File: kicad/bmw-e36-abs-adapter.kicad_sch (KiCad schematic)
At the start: 41 parts, among them J1 TE_9-6437287-8, J2 SWD, U1 TPSM33610S5, U2 TLV73333PQDBVRQ1, U3 STM32F042K6Ux, Y1 ECS-160-10-36Q-AES-TR

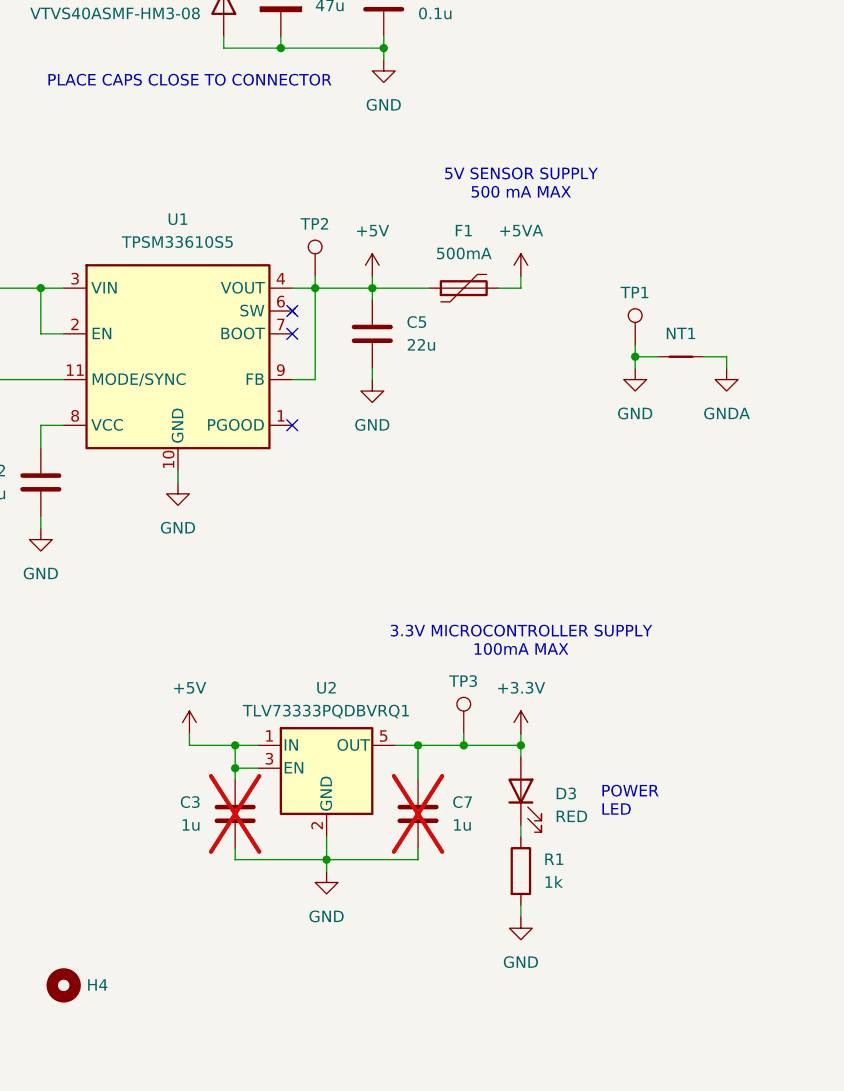
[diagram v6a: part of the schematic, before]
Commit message: Use 3.3V LDO from ADC CAN module
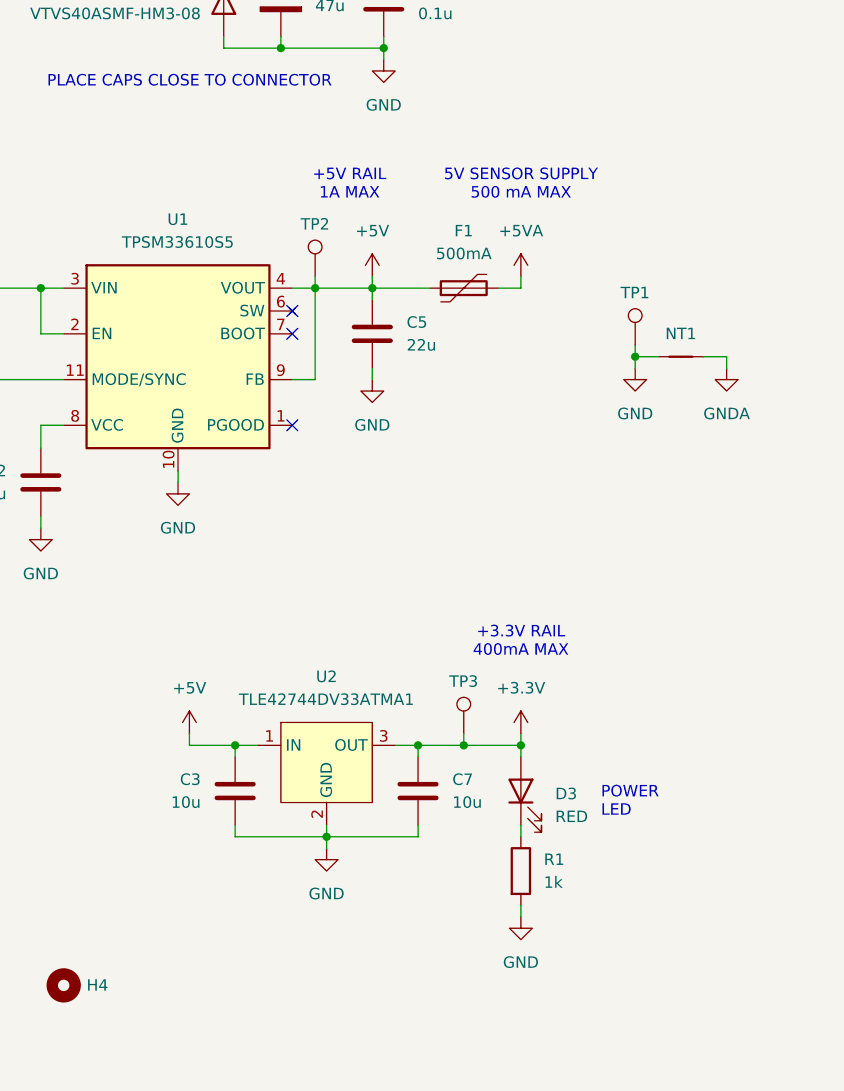
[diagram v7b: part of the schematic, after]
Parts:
- removed U2: TLV73333PQDBVRQ1, Package_TO_SOT_SMD:SOT-23-5, symbol symbols:TLV73333PDBV
- added U2: TLE42744DV33ATMA1, Package_TO_SOT_SMD:TO-252-2, symbol bmw-e36-abs-adapter:TLE42744DV33ATMA1
- C3, C7: value 1u -> 10u; footprint Capacitor_SMD:C_0603_1608Metric -> Capacitor_SMD:C_1206_3216Metric; Part Number GRT188R71E105KE13D -> GRT31CR61H106KE01L; now fitted; now in the parts list
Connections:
- net +3.3V: now also U2.3 (OUT)
- net +5V: now also U2.1 (IN)
- net GND: now also U2.2 (GND)
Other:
- note added: "+3.3V RAIL 400mA MAX"
- note added: "+5V RAIL 1A MAX"
- note removed: "3.3V MICROCONTROLLER SUPPLY 100mA MAX"

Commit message: Initial placement on PCB
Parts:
- TP1: footprint TestPoint:TestPoint_Pad_D2.0mm -> TestPoint:TestPoint_Keystone_5000-5004_Miniature
- TP2, TP3: footprint TestPoint:TestPoint_Pad_D2.0mm -> TestPoint:TestPoint_Pad_D1.5mm
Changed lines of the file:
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@@
 			)
 		)
-		(property "Footprint" "TestPoint:TestPoint_Pad_D2.0mm"
+		(property "Footprint" "TestPoint:TestPoint_Keystone_5000-5004_Miniature"
 			(at 132.08 182.88 0)
 			(hide yes)
@@
 			)
 		)
-		(property "Footprint" "TestPoint:TestPoint_Pad_D2.0mm"
+		(property "Footprint" "TestPoint:TestPoint_Pad_D1.5mm"
 			(at 113.03 226.06 0)
 			(hide yes)
@@
 			)
 		)
-		(property "Footprint" "TestPoint:TestPoint_Pad_D2.0mm"
+		(property "Footprint" "TestPoint:TestPoint_Pad_D1.5mm"
 			(at 96.52 175.26 0)
 			(hide yes)
